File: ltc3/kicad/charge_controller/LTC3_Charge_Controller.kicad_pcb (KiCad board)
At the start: 4 copper layers, 91.4 x 88.5 mm, 117 parts, among them P1 MicroFit header, P2 MicroFit header, P3 S2BPHKS, P4 MicroFit header, Q1 ZVN4525E6, Q2 BSC028N06NS, Q3 BSC028N06NS, Q4 BSC028N06NS, Q5 BSC028N06NS, Q6 ZVP3310F, Q7 MMBT5550L, U1 PI2127, U2 PI2127, U3 LT8490, U4 LTC2990

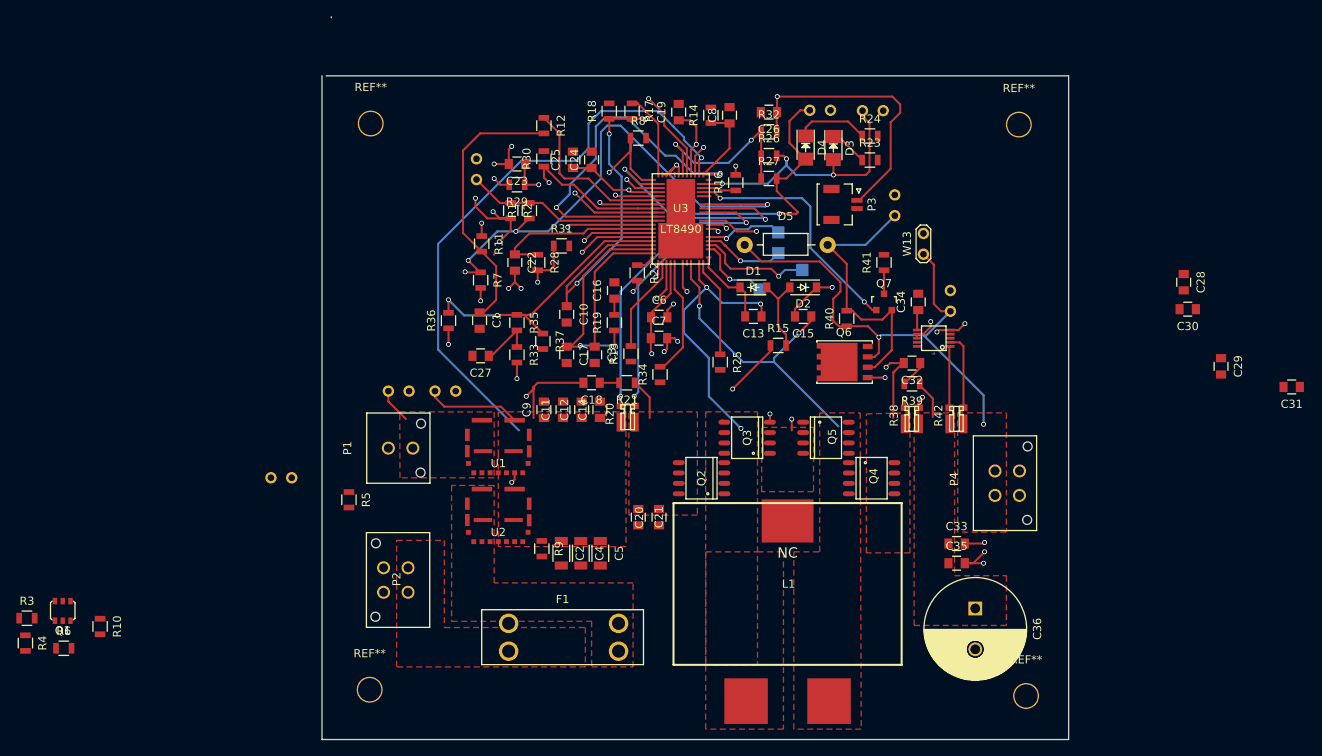
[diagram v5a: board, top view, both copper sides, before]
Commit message: LTC3: Rev 0.1 of LTC3 Charge Controller Layout
Finished new revision of LTC3 charge controller layout, featuring:

-giant inductor footprint (squid)
-mounting holes
-thermal relief turned off for Vin
-Vout connector
-surface mount LEDs
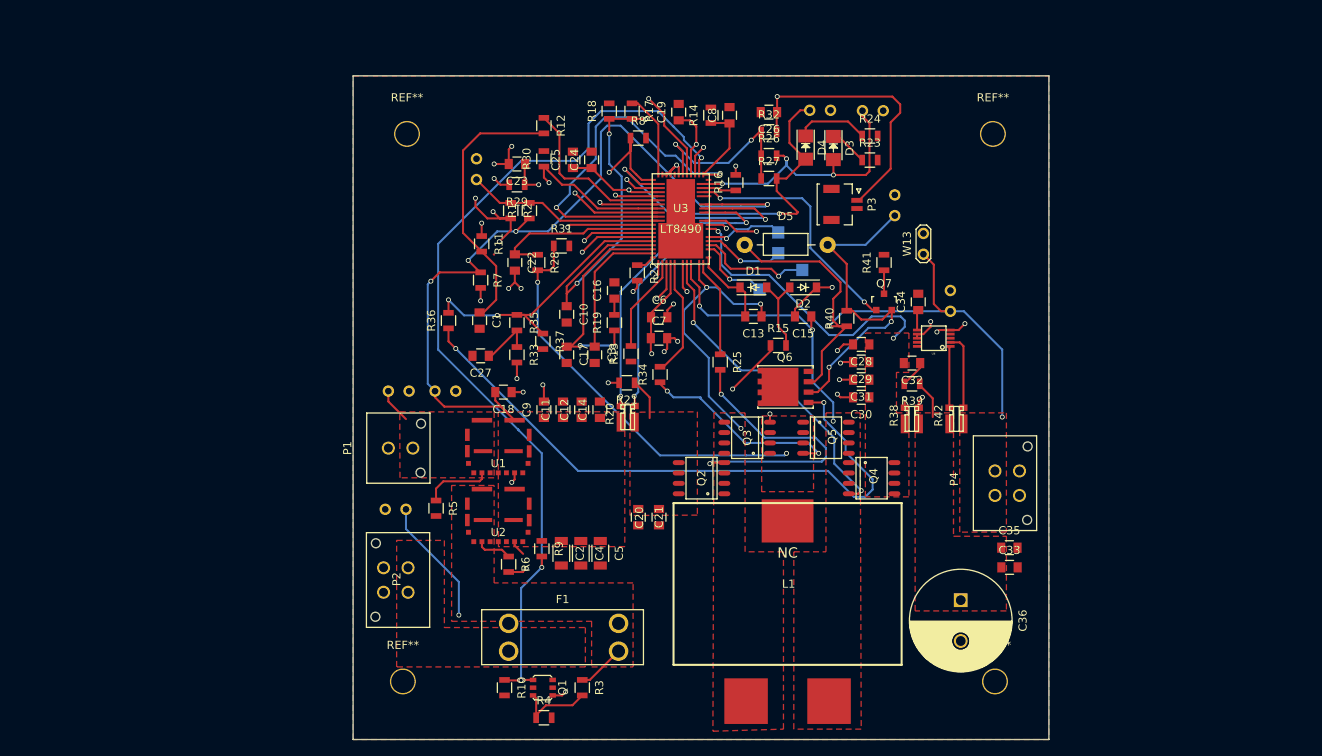
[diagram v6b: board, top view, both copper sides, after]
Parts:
- moved R3 68.5 mm to (127.1, 137.2), turned to 270 degrees
- moved R4 64.2 mm to (122.4, 140.8), turned to 0 degrees
- moved Q1 59.5 mm to (122.3, 137.2), turned to 270 degrees
- moved R6 55.4 mm to (118.1, 122.0), turned to 270 degrees
- moved C31 52.7 mm to (161.3, 99.4)
- moved R10 50.1 mm to (117.6, 137.2)
- moved C29 44.1 mm to (161.3, 97.3), turned to 180 degrees
- moved C30 41.4 mm to (161.3, 101.6)
- moved C28 40.2 mm to (161.3, 95.1), turned to 180 degrees
- moved W1 14.5 mm to (103.0, 115.3)
- moved C18 10.9 mm to (117.5, 101.0)
- moved R5 10.7 mm to (109.2, 115.2)
- moved Q6 7.85 mm to (152.0, 100.3)
- moved C33 7.11 mm to (179.5, 122.4)
- moved C35 6.74 mm to (179.4, 120.0)
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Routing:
- net /TG2: track 0.00 -> 40.4 mm, vias 0 -> 2
- net Net-(Q1-Pad1): track 72.5 -> 110.4 mm, vias 1 -> 3
- net /TG1: track 0.00 -> 36.1 mm, vias 0 -> 2
- net /BG2: track 0.00 -> 25.1 mm, vias 0 -> 2
- net Net-(F1-Pad2): track 0.00 -> 21.5 mm, vias 0 -> 1
- net /EXTVCC: track 50.2 -> 35.6 mm
- net Net-(D5-Pad1): track 61.8 -> 73.7 mm
- net Net-(C18-Pad1): track 2.37 -> 13.6 mm, vias 0 -> 2
- net Net-(Q3-Pad1): track 59.6 -> 49.1 mm
- net Net-(Q6-Pad1): track 66.6 -> 76.8 mm
- net Net-(Q1-Pad3): track 0.00 -> 9.86 mm
- net VIN: track 107.3 -> 98.5 mm, vias 5 -> 4
- net Net-(R5-Pad1): track 0.05 -> 8.37 mm
- net GND: track 67.0 -> 74.9 mm, vias 22 -> 26
- net Net-(D5-Pad2): track 33.9 -> 41.3 mm, vias 0 -> 2
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- added copper zone on F.Cu, net GND
- added copper zone on Ground.Plane, net GND
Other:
- board size 91.4 x 88.5 mm -> 85.2 x 81.3 mm

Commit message: LTC3: Cell Protection Layout
Made significant progress of Cell Protection board layout,
connected most nodes and began creating ground planes.

Reorganized mounting holes on Charge Controller
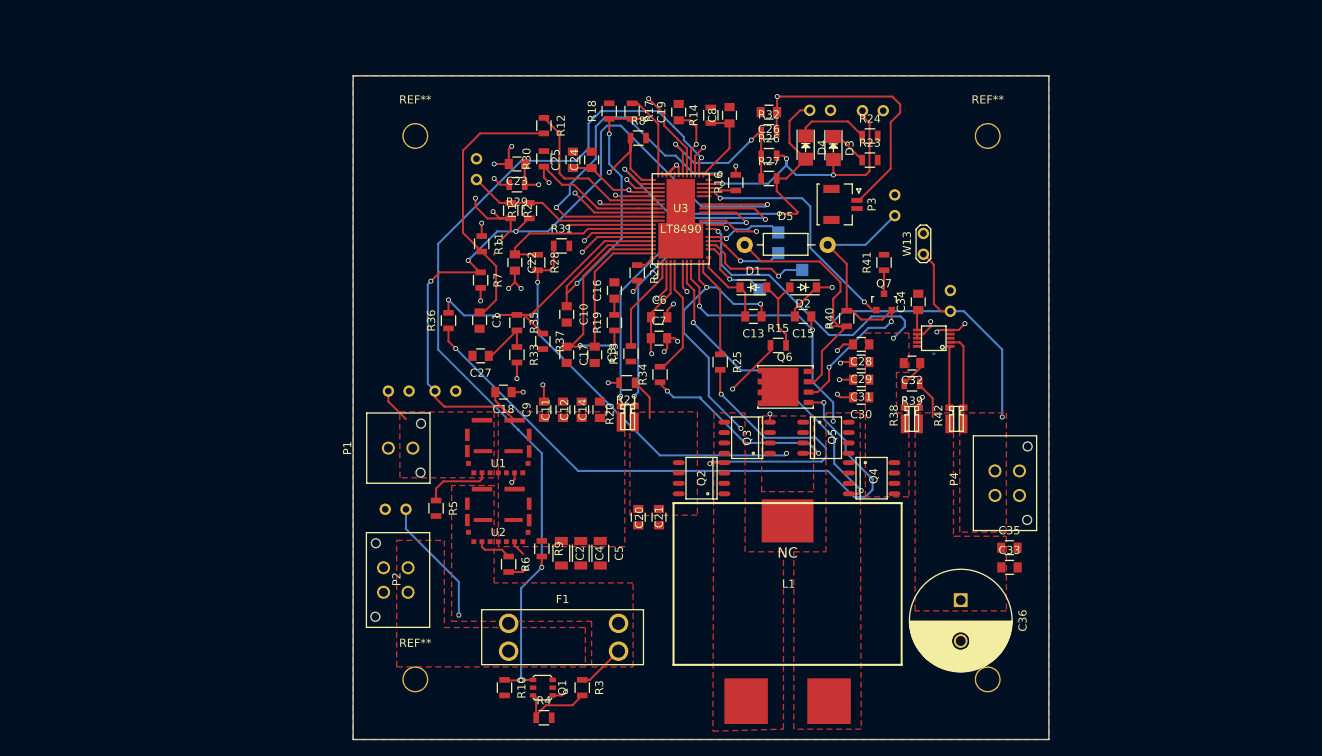
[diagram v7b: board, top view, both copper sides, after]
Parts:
- moved REF** 1.55 mm to (106.7, 136.1)
- moved REF** 1.05 mm to (106.7, 69.6)
- moved REF** 0.92 mm to (176.8, 136.1)
- moved REF** 0.68 mm to (176.8, 69.6)
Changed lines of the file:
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@@
     (links 264)
     (no_connects 0)
-    (area 94.780972 62.179999 190.461029 144.0641)
+    (area 94.780972 62.179999 188.048029 144.0641)
     (thickness 1.6)
     (drawings 4)
@@
     (0 F.Cu signal)
     (1 Ground.Plane signal hide)
-    (2 In2.Cu signal)
-    (31 B.Cu signal)
+    (2 In2.Cu signal hide)
+    (31 B.Cu signal hide)
     (32 B.Adhes user)
     (33 F.Adhes user)
@@
   )
   (module LTC3:MountingHole_0.1120in_number4 (layer F.Cu)
-    (at 105.156 136.398)
+    (at 106.68 136.144)
     (descr "Mounting Hole 0.1120in, no annular, #4")
     (tags "mounting hole 0.1120 no annular #4")
@@
   )
   (module LTC3:MountingHole_0.1120in_number4 (layer F.Cu)
-    (at 177.673 136.398)
+    (at 176.784 136.144)
     (descr "Mounting Hole 0.1120in, no annular, #4")
     (tags "mounting hole 0.1120 no annular #4")
@@
   )
   (module LTC3:MountingHole_0.1120in_number4 (layer F.Cu)
-    (at 177.419 69.342)
+    (at 176.784 69.596)
     (descr "Mounting Hole 0.1120in, no annular, #4")
     (tags "mounting hole 0.1120 no annular #4")
@@
   )
   (module LTC3:MountingHole_0.1120in_number4 (layer F.Cu)
-    (at 105.664 69.342)
+    (at 106.68 69.596)
     (descr "Mounting Hole 0.1120in, no annular, #4")
     (tags "mounting hole 0.1120 no annular #4")

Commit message: LTC3: Layout Work/Connector Updating
Added many needed connectors and added to layout.

	-Added 5V nodes for Charge Controller/Cell Protection
	-Added I2C bus connectors
	-Added Vin connectors for Cell Protection

Added all connectors to layout and ensured all nodes were connected.
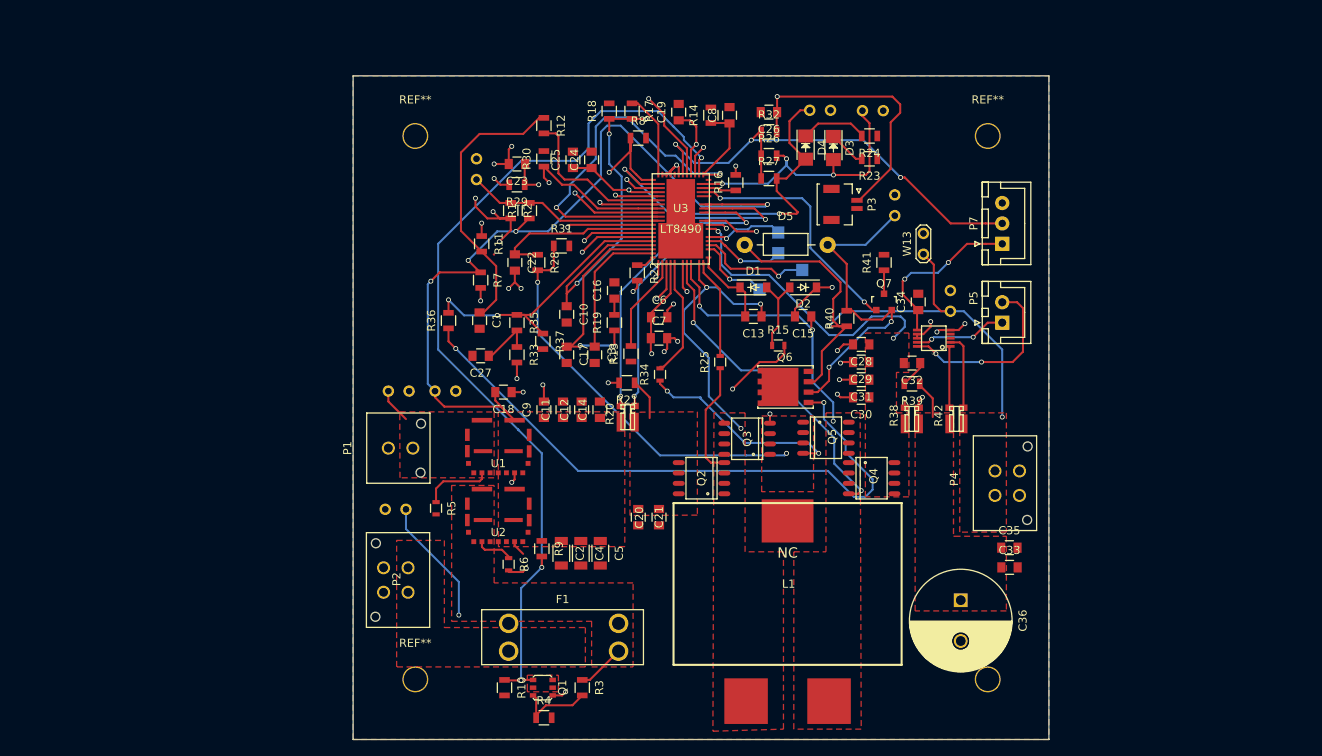
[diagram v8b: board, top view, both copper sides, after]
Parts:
- added P5: JST XH header, Connectors_JST:JST_XH_B02B-XH-A_02x2.50mm_Straight, F.Cu at (178.6, 92.5)
- added P7: JST XH header, Connectors_JST:JST_XH_B03B-XH-A_03x2.50mm_Straight, F.Cu at (178.6, 82.8)
- R15, R25, R34, R5, R6: footprint Resistors_SMD:R_0805 -> Resistors_SMD:R_0603
- moved R23 0.16 mm to (162.3, 72.4), turned to 180 degrees
- moved Q3 0.13 mm to (147.3, 106.7)
- moved R24 0.05 mm to (162.3, 69.6), turned to 180 degrees
- turned R25 to 90 degrees
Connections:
- net Net-(D5-Pad1) renamed /VBATT
- Q1 pad 2: (no net) -> Net-(Q1-Pad1)
- Q1 pad 5: (no net) -> Net-(Q1-Pad1)
- Q1 pad 6: (no net) -> Net-(Q1-Pad1)
- Q4 pad 1: /SW2 -> (no net)
- Q4 pad 2: /SW2 -> (no net)
- R12 pad 1: Net-(R12-Pad1) -> Net-(C1-Pad1)
- R12 pad 2: Net-(C1-Pad1) -> Net-(R12-Pad2)
- R15 pad 1: Net-(C6-Pad1) -> Net-(D1-Pad2)
- R15 pad 2: Net-(D1-Pad2) -> Net-(C6-Pad1)
- R23 pad 1: Net-(D3-Pad1) -> GND
- R23 pad 2: GND -> Net-(D3-Pad1)
- R24 pad 1: Net-(D4-Pad1) -> GND
- R24 pad 2: GND -> Net-(D4-Pad1)
- R25 pad 1: Net-(R25-Pad1) -> /TG1
- R25 pad 2: /TG1 -> Net-(R25-Pad2)
- U3 pad 32: Net-(R25-Pad1) -> Net-(R25-Pad2)
- U3 pad 6: Net-(R12-Pad1) -> Net-(R12-Pad2)
- U4 pad 6: (no net) -> /I2C_DATA
- U4 pad 7: (no net) -> /I2C_CLOCK
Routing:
- net +3V3: track 62.4 -> 97.3 mm, vias 4 -> 5
- net /I2C_DATA: track 0.00 -> 22.5 mm, vias 0 -> 2
- net /TG1: track 36.1 -> 14.2 mm, vias 2 -> 0
- net Net-(R12-Pad1): track 21.0 -> 0.00 mm
- net Net-(R12-Pad2): track 0.00 -> 20.0 mm
- net +5V: track 2.51 -> 20.9 mm, vias 0 -> 2
- net Net-(R25-Pad2): track 0.00 -> 12.3 mm
- net Net-(R25-Pad1): track 12.1 -> 0.00 mm
- net /I2C_CLOCK: track 0.00 -> 11.4 mm, vias 0 -> 2
- net Net-(C6-Pad1): track 63.3 -> 65.2 mm
- net Net-(C1-Pad1): track 33.4 -> 34.4 mm
- net Net-(D4-Pad1): track 9.02 -> 8.30 mm
- added copper zone on F.Cu, net Net-(Q1-Pad1)
